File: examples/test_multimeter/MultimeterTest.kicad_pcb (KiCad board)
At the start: 4 copper layers, 145 x 18 mm, 110 parts, among them sw1 3.9x2.9mm Switch, sw2 3.9x2.9mm Switch

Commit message: Update MultimeterTest.kicad_pcb
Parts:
- moved measure.range.switch.sw[0_0].ic 34.7 mm to (62.0, 2.00)
- moved measure.range.switch.sw[0_0].vdd_cap 34.7 mm to (62.0, 2.00)
- moved measure.range.switch.sw[0_1].ic 34.7 mm to (62.0, -2.00)
- moved measure.range.switch.sw[0_1].vdd_cap 34.7 mm to (62.0, -2.00)
- moved measure.range.switch.sw[1_0].ic 34.7 mm to (66.0, 0.00)
- moved measure.range.switch.sw[1_0].vdd_cap 34.7 mm to (66.0, 0.00)
- moved measure.range.res[0] 34.0 mm to (58.0, 3.00)
- moved measure.range.res[1] 34.0 mm to (58.0, 1.00)
- moved measure.range.res[2] 34.0 mm to (58.0, -1.00)
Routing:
- net mcu.gpio.measure_select_0_0: track 0.00 -> 6.74 mm, vias 0 -> 2
- net driver.select.0_0: track 0.00 -> 6.74 mm, vias 0 -> 2
- net measure.range.switch.sw[1_0].inputs.0: track 0.00 -> 3.51 mm
- net driver.range.switch.sw[1_0].inputs.0: track 0.00 -> 3.51 mm
- net measure.range.switch.sw[1_0].inputs.1: track 0.00 -> 2.39 mm
- net driver.range.switch.sw[1_0].inputs.1: track 0.00 -> 2.39 mm
- net measure.range.switch.inputs.2: track 0.00 -> 2.37 mm, vias 0 -> 1
- net measure.range.switch.inputs.1: track 0.00 -> 2.37 mm, vias 0 -> 1
- net measure.range.switch.inputs.0: track 0.00 -> 2.37 mm, vias 0 -> 1
- net driver.range.switch.inputs.3: track 0.00 -> 2.37 mm, vias 0 -> 1
- net driver.range.switch.inputs.2: track 0.00 -> 2.37 mm, vias 0 -> 1
- net driver.range.switch.inputs.1: track 0.00 -> 2.37 mm, vias 0 -> 1
- net driver.range.switch.inputs.0: track 0.00 -> 2.37 mm, vias 0 -> 1
- net vanalog: vias 7 -> 6

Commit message: Update MultimeterTest.kicad_pcb
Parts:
- moved ref_buf.ic 156.8 mm to (40.1, 3.00)
- moved inn_mux.ic 156.7 mm to (41.0, -4.00)
- moved ref_buf.vdd_cap 155.5 mm to (40.0, 3.00)
- moved inn_mux.vdd_cap 154.3 mm to (41.0, -4.00)
- moved adc.avdd_cap_0 31.0 mm to (159.0, -26.0)
- moved adc.avdd_cap_1 31.0 mm to (159.0, -24.0)
- moved adc.avdd_res 31.0 mm to (159.0, -22.0)
- moved adc.dvdd_cap_0 31.0 mm to (163.0, -26.0)
- moved adc.dvdd_cap_1 31.0 mm to (163.0, -24.0)
- moved adc.dvdd_res 31.0 mm to (163.0, -22.0)
- moved adc.ic 31.0 mm to (161.0, -22.5)
- moved adc.vref_cap 31.0 mm to (159.0, -19.0)
- moved tp_vref 31.0 mm to (163.0, -19.0)
- moved tp_3v3 21.3 mm to (111.0, -18.0)
- moved tp_5v 21.3 mm to (115.0, -18.0)
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
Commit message: Update MultimeterTest.kicad_pcb
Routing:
- net ref_div.output: track 8.10 -> 3.76 mm, vias 1 -> 0
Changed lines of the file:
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@@
     (thickness 1.6)
     (drawings 16)
-    (tracks 393)
+    (tracks 388)
     (zones 0)
     (modules 110)
@@
   (segment (start 162.175 -22) (end 162.175 -22.825) (width 0.25) (layer B.Cu) (net 2))
   (segment (start 162.175 -22.825) (end 162 -23) (width 0.25) (layer B.Cu) (net 2))
-  (segment (start 190.9 41.05) (end 191.318002 41.05) (width 0.25) (layer F.Cu) (net 3))
   (segment (start 156.15 41.75) (end 155.25 41.75) (width 0.25) (layer F.Cu) (net 54))
   (segment (start 156.175 46) (end 155.5 46) (width 0.25) (layer B.Cu) (net 54))
@@
   (segment (start 189 45.5) (end 188.5 45) (width 0.25) (layer B.Cu) (net 50))
   (segment (start 187.825 45) (end 188.5 45) (width 0.25) (layer B.Cu) (net 50))
-  (via (at 189 46) (size 0.7) (drill 0.3) (layers F.Cu B.Cu) (net 50))
   (segment (start 189 45.5) (end 189 46) (width 0.25) (layer B.Cu) (net 50))
   (segment (start 189 46) (end 189 46.5) (width 0.25) (layer B.Cu) (net 50))
-  (segment (start 190.9 42.95) (end 190.05 42.95) (width 0.25) (layer F.Cu) (net 50))
-  (segment (start 189 44) (end 189 46) (width 0.25) (layer F.Cu) (net 50))
-  (segment (start 190.05 42.95) (end 189 44) (width 0.25) (layer F.Cu) (net 50))
   (via (at 104 36) (size 0.7) (drill 0.3) (layers F.Cu B.Cu) (net 49))
   (segment (start 104.35 35.65) (end 104 36) (width 0.25) (layer F.Cu) (net 49))

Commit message: booster layout
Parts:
- moved prot_5v 23.3 mm to (89.4, -19.8)
- moved prot_analog 23.3 mm to (94.0, -12.5)
- moved reg_5v.power_path.inductor 8.00 mm to (173.0, 8.00), turned to 180 degrees
- moved driver.range.res[0] 6.00 mm to (58.0, 5.00)
- moved driver.range.res[1] 6.00 mm to (58.0, 3.00)
- moved driver.range.res[2] 6.00 mm to (58.0, 1.00)
- moved driver.range.res[3] 6.00 mm to (58.0, -1.00)
- moved driver.range.switch.sw[0_0].ic 6.00 mm to (62.0, 4.00)
- moved driver.range.switch.sw[0_0].vdd_cap 6.00 mm to (62.0, 4.00)
- moved driver.range.switch.sw[0_1].ic 6.00 mm to (62.0, 0.00)
- moved driver.range.switch.sw[0_1].vdd_cap 6.00 mm to (62.0, 0.00)
- moved driver.range.switch.sw[1_0].ic 6.00 mm to (66.0, 2.00)
- moved driver.range.switch.sw[1_0].vdd_cap 6.00 mm to (66.0, 2.00)
- moved measure.range.res[0] 6.00 mm to (58.0, -3.00)
- moved measure.range.res[1] 6.00 mm to (58.0, -5.00)
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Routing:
- net vbatsense.input: track 0.00 -> 10.9 mm, vias 0 -> 2
- net gnd: track 50.4 -> 60.3 mm, vias 10 -> 14
- net reg_5v.ce_res.io: track 0.00 -> 7.17 mm, vias 0 -> 1
- net reg_5v.power_path.switch: track 0.00 -> 3.71 mm, vias 0 -> 1
- net v5v: track 9.06 -> 12.4 mm, vias 2 -> 3

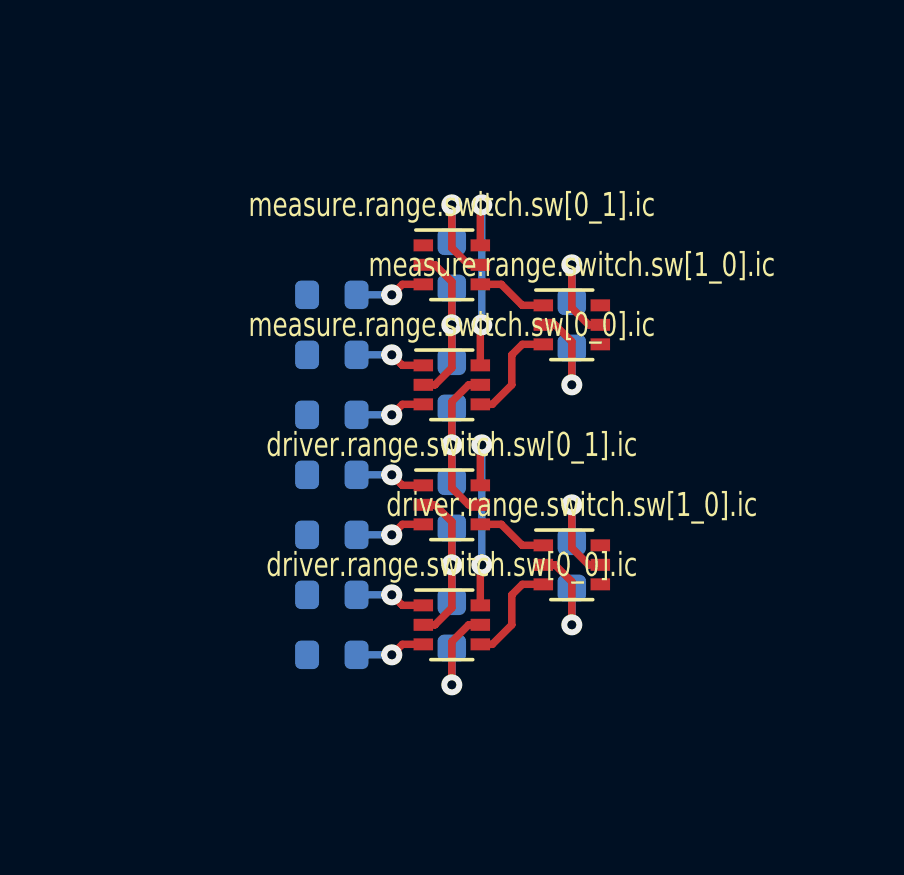
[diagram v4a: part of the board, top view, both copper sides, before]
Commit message: compact switch routing
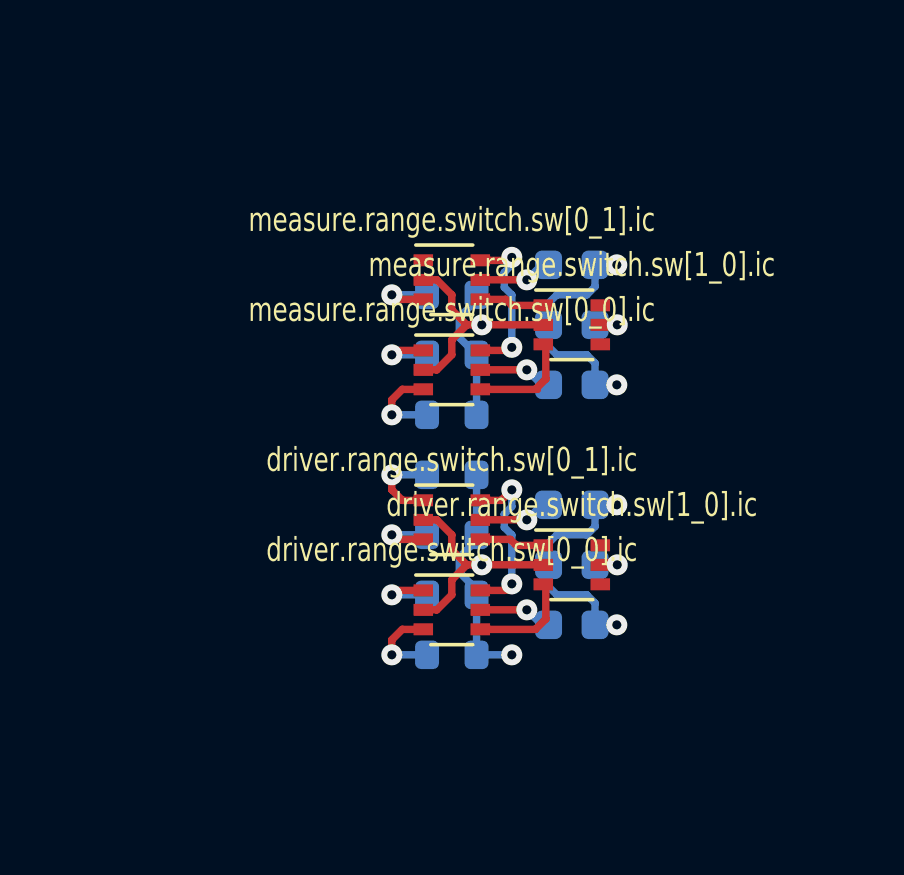
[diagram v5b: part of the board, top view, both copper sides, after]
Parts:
- moved driver.range.res[0] 4.00 mm to (62.0, 5.00), turned to 180 degrees
- moved driver.range.res[1] 4.00 mm to (62.0, 3.00), turned to 180 degrees
- moved driver.range.res[2] 4.00 mm to (62.0, 1.00), turned to 180 degrees
- moved driver.range.res[3] 4.00 mm to (62.0, -1.00), turned to 180 degrees
- moved driver.range.switch.sw[0_0].vdd_cap 4.00 mm to (66.0, 4.00), turned to 0 degrees
- moved driver.range.switch.sw[0_1].vdd_cap 4.00 mm to (66.0, 0.00), turned to 0 degrees
- moved measure.range.res[0] 4.00 mm to (62.0, -3.00), turned to 180 degrees
- moved measure.range.res[1] 4.00 mm to (62.0, -5.00), turned to 180 degrees
- moved measure.range.res[2] 4.00 mm to (62.0, -7.00), turned to 180 degrees
- moved measure.range.switch.sw[0_0].vdd_cap 4.00 mm to (66.0, -4.00), turned to 0 degrees
- moved measure.range.switch.sw[0_1].vdd_cap 4.00 mm to (66.0, -8.00), turned to 0 degrees
- moved driver.range.switch.sw[0_0].ic 0.50 mm to (62.0, 3.50)
- moved driver.range.switch.sw[0_1].ic 0.50 mm to (62.0, 0.50)
- moved measure.range.switch.sw[0_0].ic 0.50 mm to (62.0, -4.50)
- moved measure.range.switch.sw[0_1].ic 0.50 mm to (62.0, -7.50)
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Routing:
- net gnd: track 60.3 -> 67.6 mm, vias 14 -> 16
- net inn_merge.inputs.1: track 0.00 -> 4.48 mm
- net vanalog: track 24.3 -> 21.6 mm, vias 6 -> 8
- net mcu.gpio.measure_select_0_0: track 6.74 -> 5.39 mm
- net driver.select.0_0: track 6.74 -> 5.68 mm
- net measure.range.switch.inputs.0: track 2.37 -> 2.87 mm
- net driver.range.switch.inputs.3: track 2.37 -> 2.87 mm
- net driver.range.switch.inputs.0: track 2.37 -> 2.87 mm

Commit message: Update MultimeterTest.kicad_pcb
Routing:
- net gnd: track 67.6 -> 60.3 mm, vias 16 -> 20
- net driver.select.0_0: track 5.68 -> 1.22 mm, vias 2 -> 1
- net mcu.gpio.measure_select_0_0: track 5.39 -> 1.22 mm, vias 2 -> 1
- net vanalog: track 21.6 -> 19.9 mm, vias 8 -> 7
- net driver.range.switch.sw[1_0].inputs.0: track 3.52 -> 4.44 mm
- net measure.range.switch.sw[1_0].inputs.0: track 3.55 -> 4.44 mm

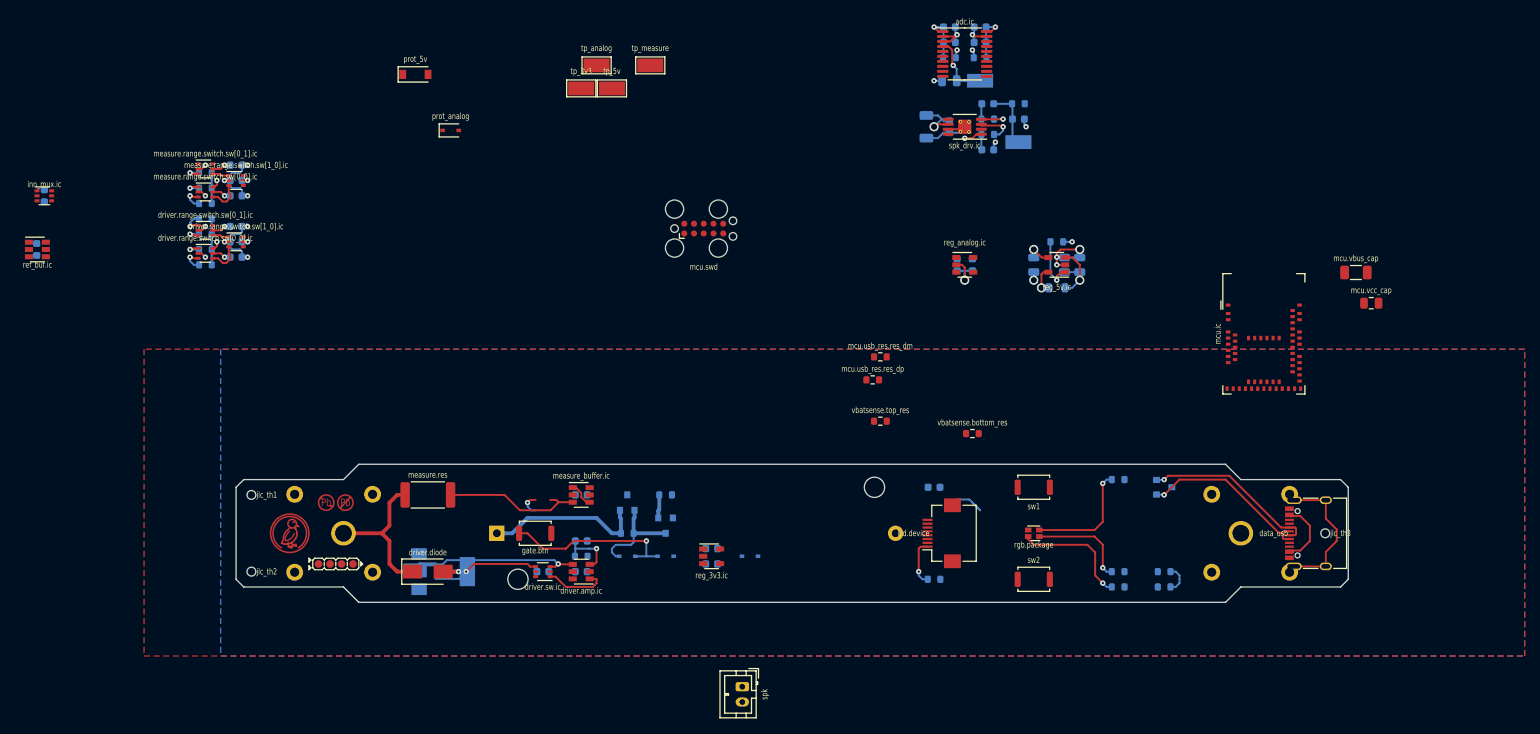
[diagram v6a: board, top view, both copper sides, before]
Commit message: compactify ranging circuits
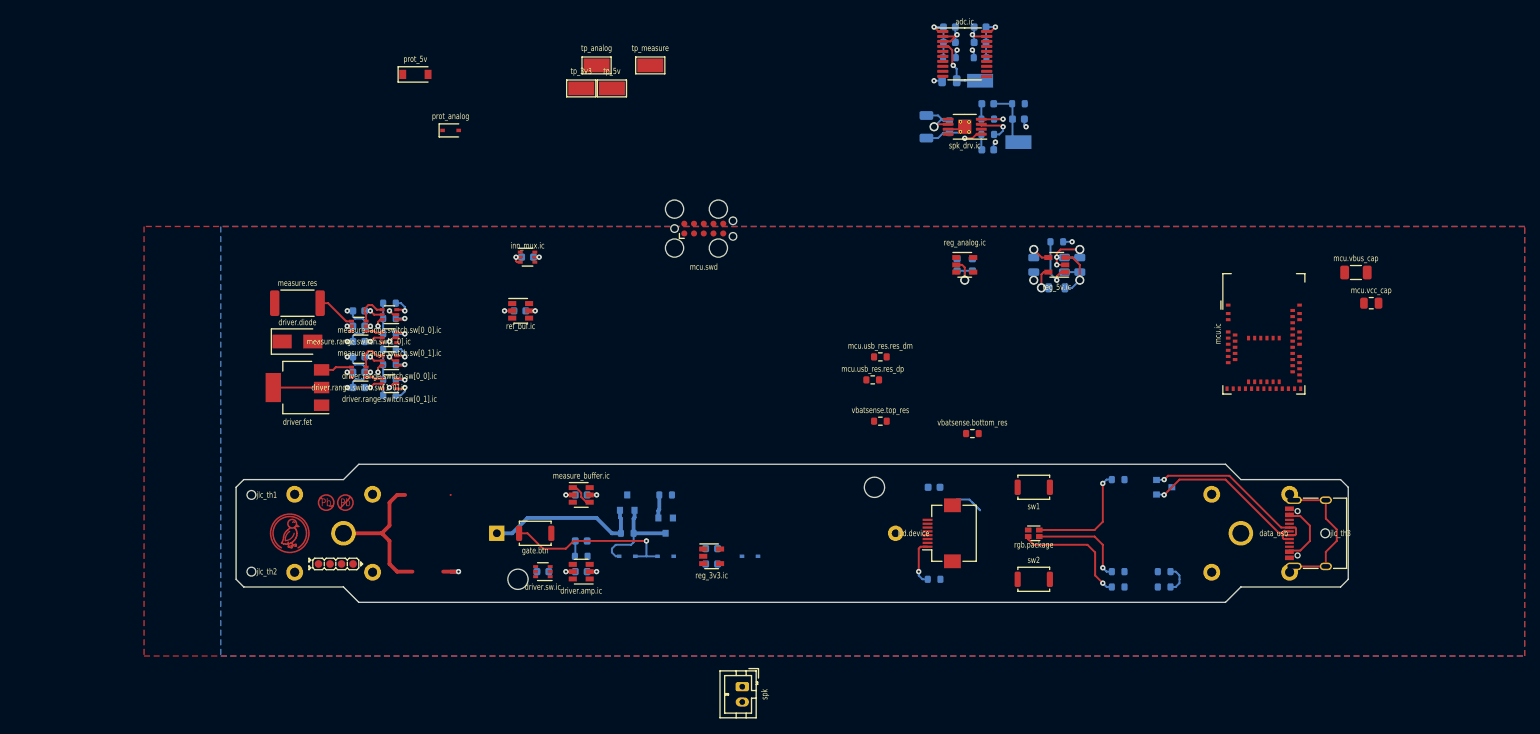
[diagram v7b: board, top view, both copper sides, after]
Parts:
- driver.fet: moved to F.Cu
- moved inn_mux.ic 63.5 mm to (104.0, 4.00)
- moved inn_mux.vdd_cap 63.5 mm to (104.0, 4.00), turned to 180 degrees
- moved ref_buf.vdd_cap 63.5 mm to (103.0, 11.0), turned to 180 degrees
- moved ref_buf.ic 63.5 mm to (103.1, 11.0)
- moved driver.diode 34.5 mm to (74.0, 15.0)
- moved driver.range.res[3] 33.2 mm to (86.0, 22.0), turned to 0 degrees
- moved measure.range.switch.sw[0_1].ic 32.6 mm to (86.0, 14.5), turned to 180 degrees
- moved measure.range.res[2] 31.9 mm to (86.0, 14.0), turned to 0 degrees
- moved driver.range.switch.sw[0_1].ic 31.2 mm to (86.0, 20.5), turned to 180 degrees
- moved driver.fet 30.6 mm to (74.0, 21.0), turned to 180 degrees
- moved driver.range.res[2] 30.6 mm to (86.0, 20.0), turned to 0 degrees
- moved measure.res 30.2 mm to (74.0, 10.0)
- moved measure.range.res[1] 29.4 mm to (86.0, 12.0), turned to 0 degrees
- moved measure.range.switch.sw[0_0].ic 28.8 mm to (86.0, 11.5), turned to 180 degrees
- moved driver.range.res[1] 28.3 mm to (86.0, 18.0), turned to 0 degrees
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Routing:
- net driver.sw.inputs.0: track 23.6 -> 4.04 mm, vias 1 -> 0
- net driver.(adapter)fet.gate.src: track 14.0 -> 0.00 mm, vias 1 -> 0
- net measure_buffer.inp: track 18.5 -> 5.11 mm
- net gnd: track 60.3 -> 69.1 mm, vias 20 -> 24
- net driver.sw.inputs.1: track 8.24 -> 0.00 mm
- net vanalog: track 19.9 -> 27.5 mm, vias 7 -> 11
- net driver.fet.drain: track 3.00 -> 9.30 mm
- net driver.control: track 7.57 -> 2.02 mm, vias 1 -> 0
- net measure.range.inputs.0: track 3.08 -> 0.00 mm, vias 1 -> 0

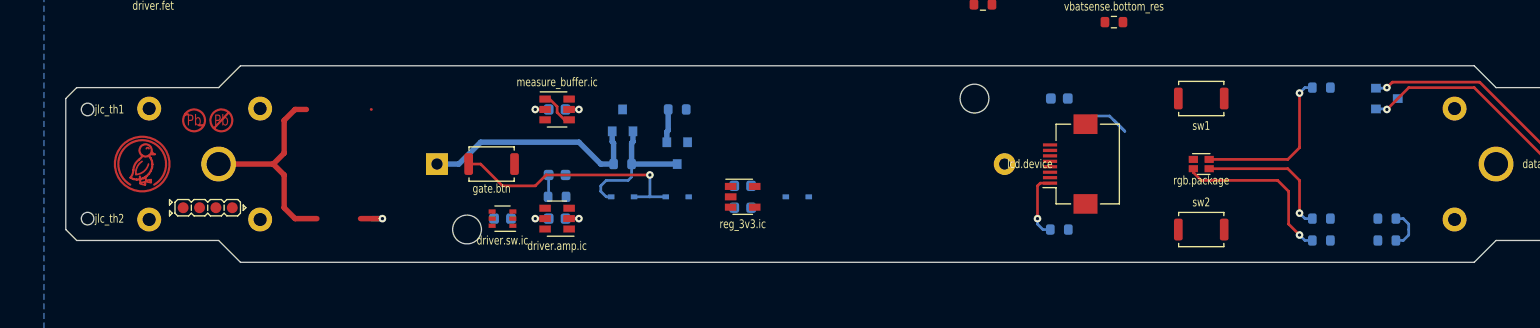
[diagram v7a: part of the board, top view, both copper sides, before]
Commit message: cleaner board outline
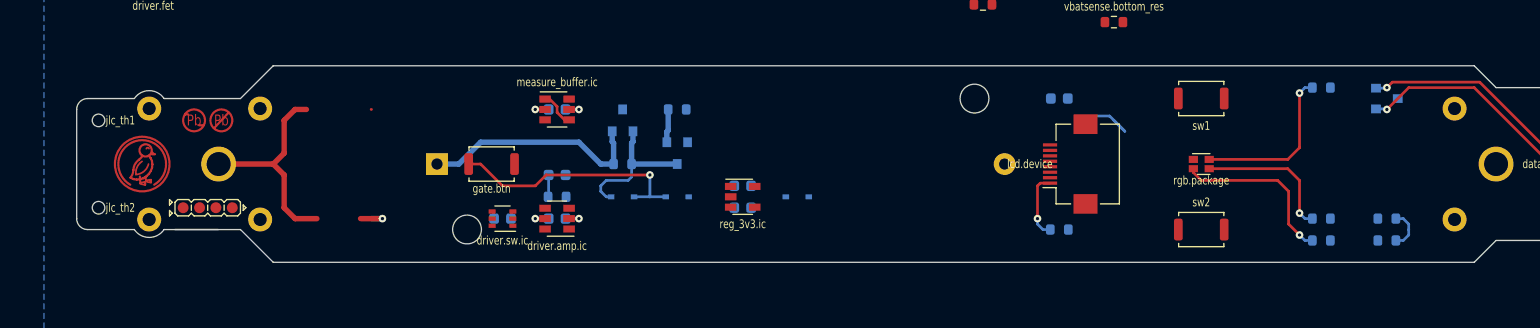
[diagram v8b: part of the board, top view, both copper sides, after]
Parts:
- moved jlc_th1 1.41 mm to (69.0, 36.0)
- moved jlc_th2 1.41 mm to (69.0, 44.0)
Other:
- board size 145 x 18 mm -> 144 x 18 mm
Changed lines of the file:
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@@
   (general
     (thickness 1.6)
-    (drawings 16)
+    (drawings 21)
     (tracks 451)
     (zones 0)
@@
   )
   (module edg:JlcToolingHole_1.152mm (layer F.Cu)
-    (at 68 35)
+    (at 69 36)
     (descr "Tooling holes for JLC assembly, 1.152 mm hole + 1.3mm soldermask opening")
     (path /jlc_th1)
@@
   )
   (module edg:JlcToolingHole_1.152mm (layer F.Cu)
-    (at 68 45)
+    (at 69 44)
     (descr "Tooling holes for JLC assembly, 1.152 mm hole + 1.3mm soldermask opening")
     (path /jlc_th2)
@@
     )
   )
+  (gr_line (start 68 46) (end 72.279127 46) (layer Edge.Cuts) (width 0.05))
+  (gr_line (start 80 45.999999) (end 74.998394 46) (layer Edge.Cuts) (width 0.05))
+  (gr_arc (start 73.639127 45.08) (end 72.279127 46) (angle -111.8) (layer Edge.Cuts) (width 0.05))
+  (gr_arc (start 73.64 34.92) (end 75 34) (angle -111.8) (layer Edge.Cuts) (width 0.05))
+  (gr_line (start 76 45.999999) (end 82 46) (layer Edge.Cuts) (width 0.05))
+  (gr_line (start 75 34) (end 82 34) (layer Edge.Cuts) (width 0.05))
+  (gr_arc (start 68 45) (end 67 45) (angle -90) (layer Edge.Cuts) (width 0.05))
+  (gr_arc (start 68 35) (end 68 34) (angle -90) (layer Edge.Cuts) (width 0.05))
   (gr_line (start 211 46) (end 210 47) (layer Edge.Cuts) (width 0.05))
   (gr_line (start 210 33) (end 211 34) (layer Edge.Cuts) (width 0.05))
-  (gr_line (start 66 46) (end 67 47) (layer Edge.Cuts) (width 0.05))
-  (gr_line (start 66 46) (end 66 34) (layer Edge.Cuts) (width 0.05))
-  (gr_line (start 80 47) (end 67 47) (layer Edge.Cuts) (width 0.05))
-  (gr_line (start 82 49) (end 80 47) (layer Edge.Cuts) (width 0.05))
-  (gr_line (start 195 49) (end 82 49) (layer Edge.Cuts) (width 0.05))
+  (gr_line (start 67 45) (end 67 35) (layer Edge.Cuts) (width 0.05))
+  (gr_line (start 85 49) (end 82 46) (layer Edge.Cuts) (width 0.05))
+  (gr_line (start 195 49) (end 85 49) (layer Edge.Cuts) (width 0.05))
   (gr_line (start 197 47) (end 195 49) (layer Edge.Cuts) (width 0.05))
   (gr_line (start 210 47) (end 197 47) (layer Edge.Cuts) (width 0.05))
@@
   (gr_line (start 197 33) (end 210 33) (layer Edge.Cuts) (width 0.05))
   (gr_line (start 195 31) (end 197 33) (layer Edge.Cuts) (width 0.05))
-  (gr_line (start 82 31) (end 195 31) (layer Edge.Cuts) (width 0.05))
-  (gr_line (start 82 31) (end 80 33) (layer Edge.Cuts) (width 0.05))
-  (gr_line (start 67 33) (end 80 33) (layer Edge.Cuts) (width 0.05))
-  (gr_line (start 66 34) (end 67 33) (layer Edge.Cuts) (width 0.05))
+  (gr_line (start 85 31) (end 195 31) (layer Edge.Cuts) (width 0.05))
+  (gr_line (start 85 31) (end 82 34) (layer Edge.Cuts) (width 0.05))
+  (gr_line (start 68 34) (end 72.279127 34) (layer Edge.Cuts) (width 0.05))
   (via (at 160 -25) (size 0.7) (drill 0.3) (layers F.Cu B.Cu) (net 1))
   (segment (start 159.775 -24.775) (end 160 -25) (width 0.25) (layer B.Cu) (net 1))
